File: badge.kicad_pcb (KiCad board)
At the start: 2 copper layers, 76.2 x 127 mm, 31 parts, among them J1 TC2030, SW1 SW_Push, SW2 SW_Push, SW3 SW_Push, SW4 SW_Push, SW5 SW_Push, SW6 SW_SPST, U1 NHD-C12832A1Z-FSRGB-FBW-3V, X1 Simple_Addon_v2

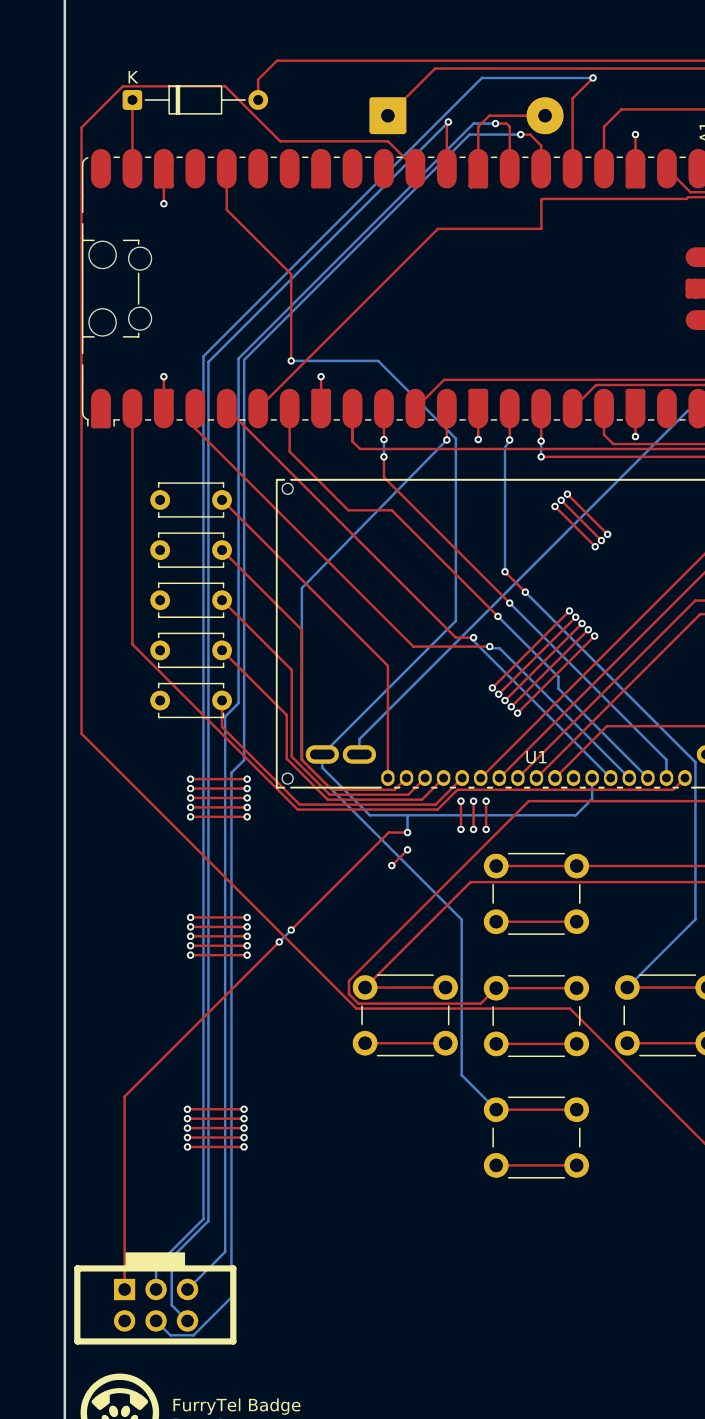
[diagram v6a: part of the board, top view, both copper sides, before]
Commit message: SAO silkscreens, nudge a few vias around
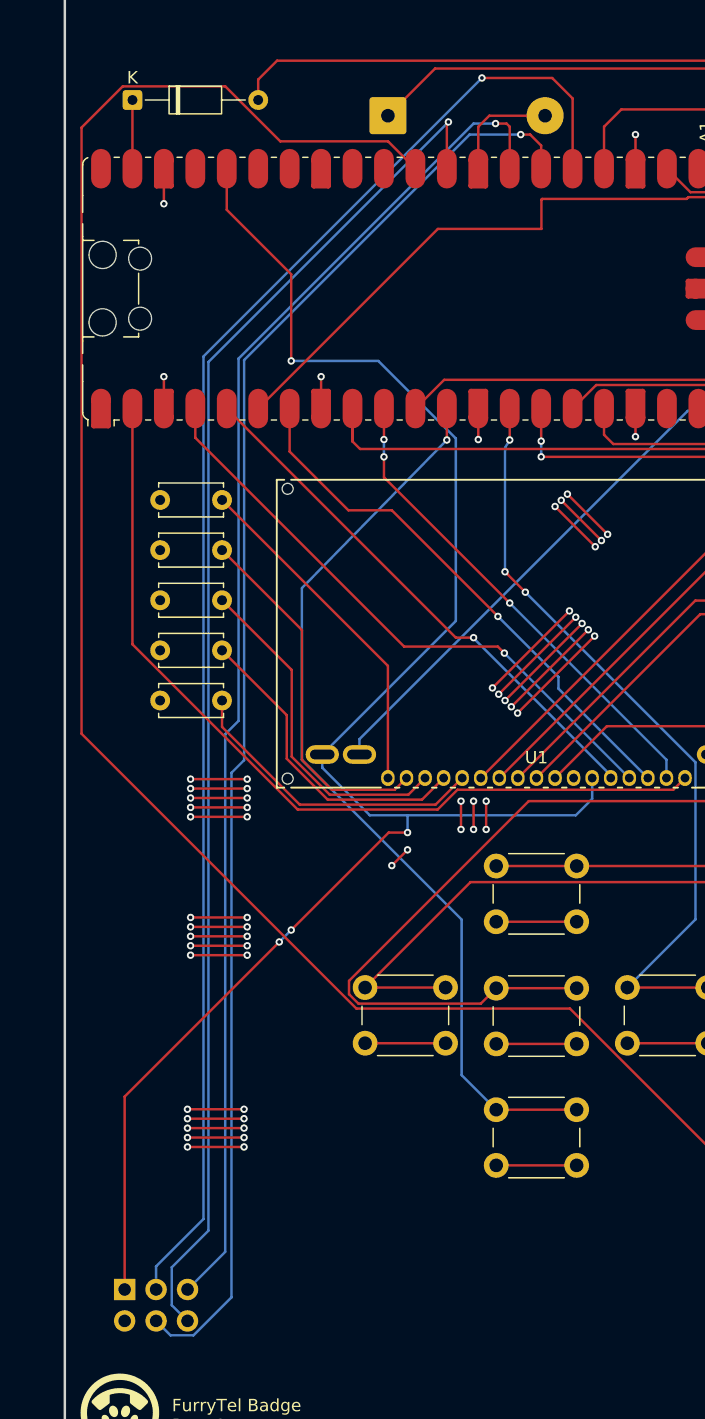
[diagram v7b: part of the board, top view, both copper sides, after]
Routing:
- net Net-(A1-GPIO19): track 125.8 -> 122.5 mm
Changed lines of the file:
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@@
 		(sheetname "/")
 		(sheetfile "badge.kicad_sch")
-		(units
-			(unit
-				(name "A")
-				(pins "1" "2" "3" "4" "5" "6")
-			)
-		)
 		(attr through_hole)
 		(duplicate_pad_numbers_are_jumpers no)
-		(fp_line
-			(start -6.3 -2.95)
-			(end 6.3 -2.95)
-			(stroke
-				(width 0.5)
-				(type solid)
-			)
-			(layer "F.SilkS")
-		)
-		(fp_line
-			(start -6.3 2.95)
-			(end -6.3 -2.95)
-			(stroke
-				(width 0.5)
-				(type solid)
-			)
-			(layer "F.SilkS")
-		)
-		(fp_line
-			(start 6.3 -2.95)
-			(end 6.3 2.95)
-			(stroke
-				(width 0.5)
-				(type solid)
-			)
-			(layer "F.SilkS")
-		)
-		(fp_line
-			(start 6.3 2.95)
-			(end -6.3 2.95)
-			(stroke
-				(width 0.5)
-				(type solid)
-			)
-			(layer "F.SilkS")
-		)
-		(fp_poly
-			(pts
-				(xy 2.3495 -3.0607) (xy -2.3495 -3.0607) (xy -2.3495 -4.2037) (xy 2.3495 -4.2037)
-			)
-			(stroke
-				(width 0.1)
-				(type solid)
-			)
-			(fill yes)
-			(layer "F.SilkS")
-		)
-		(fp_text user "VCC"
-			(at -2.54 -2.794 0)
-			(layer "B.SilkS")
-			(effects
-				(font
-					(size 0.75 0.75)
-					(thickness 0.15)
-				)
-				(justify mirror)
-			)
-		)
-		(fp_text user "GND"
-			(at -2.54 3.048 0)
-			(layer "B.SilkS")
-			(effects
-				(font
-					(size 0.75 0.75)
-					(thickness 0.15)
-				)
-				(justify mirror)
-			)
-		)
-		(fp_text user "SDA"
-			(at 0 -2.794 0)
-			(layer "B.SilkS")
-			(effects
-				(font
-					(size 0.75 0.75)
-					(thickness 0.15)
-				)
-				(justify mirror)
-			)
-		)
-		(fp_text user "SCL"
-			(at 0 3.048 0)
-			(layer "B.SilkS")
-			(effects
-				(font
-					(size 0.75 0.75)
-					(thickness 0.15)
-				)
-				(justify mirror)
-			)
-		)
-		(fp_text user "GPIO1"
-			(at 3.2 -2.794 0)
-			(layer "B.SilkS")
-			(effects
-				(font
-					(size 0.75 0.75)
-					(thickness 0.15)
-				)
-				(justify mirror)
-			)
-		)
-		(fp_text user "GPIO2"
-			(at 3.2 3.048 0)
-			(layer "B.SilkS")
-			(effects
-				(font
-					(size 0.75 0.75)
-					(thickness 0.15)
-				)
-				(justify mirror)
-			)
-		)
 		(fp_text user "${REFERENCE}"
 			(at 0 5.5 0)
@@
 	)
 	(segment
-		(start 68.072 40.132)
+		(start 59.095471 40.132)
+		(end 64.77 40.132)
+		(width 0.2)
+		(layer "F.Cu")
+		(net "Net-(A1-GPIO19)")
+	)
+	(segment
+		(start 64.77 40.132)
 		(end 66.421 41.783)
 		(width 0.2)
@@
 	)
 	(via
-		(at 68.072 40.132)
+		(at 59.095471 40.132)
 		(size 0.6)
 		(drill 0.3)
@@
 	)
 	(segment
-		(start 36.6 62.627471)
-		(end 36.6 132.31)
-		(width 0.2)
-		(layer "B.Cu")
-		(net "Net-(A1-GPIO19)")
-	)
-	(segment
-		(start 36.6 132.31)
-		(end 32.766 136.144)
+		(start 59.095471 40.132)
+		(end 36.6 62.627471)
 		(width 0.2)
 		(layer "B.Cu")
@@
 	)
 	(segment
-		(start 68.072 40.132)
-		(end 59.095471 40.132)
+		(start 36.6 132.31)
+		(end 32.766 136.144)
 		(width 0.2)
 		(layer "B.Cu")
@@
 	)
 	(segment
-		(start 59.095471 40.132)
-		(end 36.6 62.627471)
+		(start 36.6 62.627471)
+		(end 36.6 132.31)
 		(width 0.2)
 		(layer "B.Cu")
@@
 	)
 	(segment
-		(start 39.4335 62.8015)
-		(end 39.4335 90.646135)
+		(start 58.42 43.815)
+		(end 39.4335 62.8015)
 		(width 0.2)
 		(layer "B.Cu")
@@
 	)
 	(segment
-		(start 38.354 134.9627)
-		(end 35.312 138.0047)
+		(start 39.4335 92.0665)
+		(end 38.354 93.146)
 		(width 0.2)
 		(layer "B.Cu")
@@
 	)
 	(segment
-		(start 38.354 91.725635)
-		(end 38.354 134.9627)
+		(start 60.198 43.815)
+		(end 58.42 43.815)
 		(width 0.2)
 		(layer "B.Cu")
@@
 	)
 	(segment
-		(start 60.198 43.815)
-		(end 58.42 43.815)
+		(start 38.354 134.9627)
+		(end 35.312 138.0047)
 		(width 0.2)
 		(layer "B.Cu")
@@
 	)
 	(segment
-		(start 58.42 43.815)
-		(end 39.4335 62.8015)
+		(start 38.354 93.146)
+		(end 38.354 134.9627)
 		(width 0.2)
 		(layer "B.Cu")
@@
 	)
 	(segment
-		(start 39.4335 90.646135)
-		(end 38.354 91.725635)
+		(start 39.4335 62.8015)
+		(end 39.4335 92.0665)
 		(width 0.2)
 		(layer "B.Cu")
@@
 	)
 	(segment
-		(start 56.388 43.688)
-		(end 37 63.076)
+		(start 37 133.25)
+		(end 34.036 136.214)
 		(width 0.2)
 		(layer "B.Cu")
@@
 	)
 	(segment
-		(start 34.036 139.2687)
-		(end 35.312 140.5447)
+		(start 37 63.076)
+		(end 37 133.25)
 		(width 0.2)
 		(layer "B.Cu")
@@
 	)
 	(segment
-		(start 37 63.076)
-		(end 37 132.475686)
+		(start 34.036 139.2687)
+		(end 35.312 140.5447)
 		(width 0.2)
 		(layer "B.Cu")
@@
 	)
 	(segment
-		(start 34.036 135.439686)
+		(start 34.036 136.214)
 		(end 34.036 139.2687)
 		(width 0.2)
@@
 	)
 	(segment
-		(start 37 132.475686)
-		(end 34.036 135.439686)
+		(start 56.388 43.688)
+		(end 37 63.076)
 		(width 0.2)
 		(layer "B.Cu")
@@
 	)
 	(segment
-		(start 59.729715 86.066285)
-		(end 53.554285 86.066285)
+		(start 35.941 69.197)
+		(end 35.941 66.84)
 		(width 0.2)
 		(layer "F.Cu")
@@
 	)
 	(segment
-		(start 35.941 68.453)
-		(end 35.941 66.84)
+		(start 60.381185 86.066285)
+		(end 52.810285 86.066285)
 		(width 0.2)
 		(layer "F.Cu")
@@
 	)
 	(segment
-		(start 53.554285 86.066285)
-		(end 35.941 68.453)
+		(start 60.90745 86.59255)
+		(end 60.381185 86.066285)
 		(width 0.2)
 		(layer "F.Cu")
 		(net "/SCL")
 	)
-	(via
-		(at 59.729715 86.066285)
-		(size 0.6)
-		(drill 0.3)
-		(layers "F.Cu" "B.Cu")
-		(net "/SCL")
-	)
 	(segment
-		(start 71 96.6851)
-		(end 60.522607 86.207707)
+		(start 52.810285 86.066285)
+		(end 35.941 69.197)
 		(width 0.2)
-		(layer "B.Cu")
+		(layer "F.Cu")
 		(net "/SCL")
 	)
-	(segment
-		(start 59.588293 86.207707)
-		(end 59.729715 86.066285)
-		(width 0.2)
-		(layer "B.Cu")
+	(via
+		(at 60.90745 86.59255)
+		(size 0.6)
+		(drill 0.3)
+		(layers "F.Cu" "B.Cu")
 		(net "/SCL")
 	)
 	(segment
-		(start 60.522607 86.207707)
-		(end 59.588293 86.207707)
+		(start 60.90745 86.59255)
+		(end 71 96.6851)
 		(width 0.2)
 		(layer "B.Cu")
@@
 	)
 	(segment
-		(start 69.5 96.6851)
-		(end 58.42 85.6051)
+		(start 58.42 85.38755)
+		(end 58.42 85.344)
 		(width 0.2)
 		(layer "B.Cu")
@@
 	)
 	(segment
-		(start 58.42 85.6051)
-		(end 58.42 85.344)
+		(start 69.5 96.46755)
+		(end 58.42 85.38755)
+		(width 0.2)
+		(layer "B.Cu")
+		(net "/SDA")
+	)
+	(segment
+		(start 69.5 96.6851)
+		(end 69.5 96.46755)
 		(width 0.2)
 		(layer "B.Cu")
